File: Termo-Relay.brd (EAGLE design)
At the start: 53 x 75.6 mm, 45 parts, among them CN3 PBS-2-VERTICAL, CN5 PBS-4-VERTICAL, IC1 74HCT595D, IC2 74HCT595D, IC3 STM8S103FP, Q2 20M, T1 2N2222, T2 2N2222, T3 2N2222, T4 2N2222

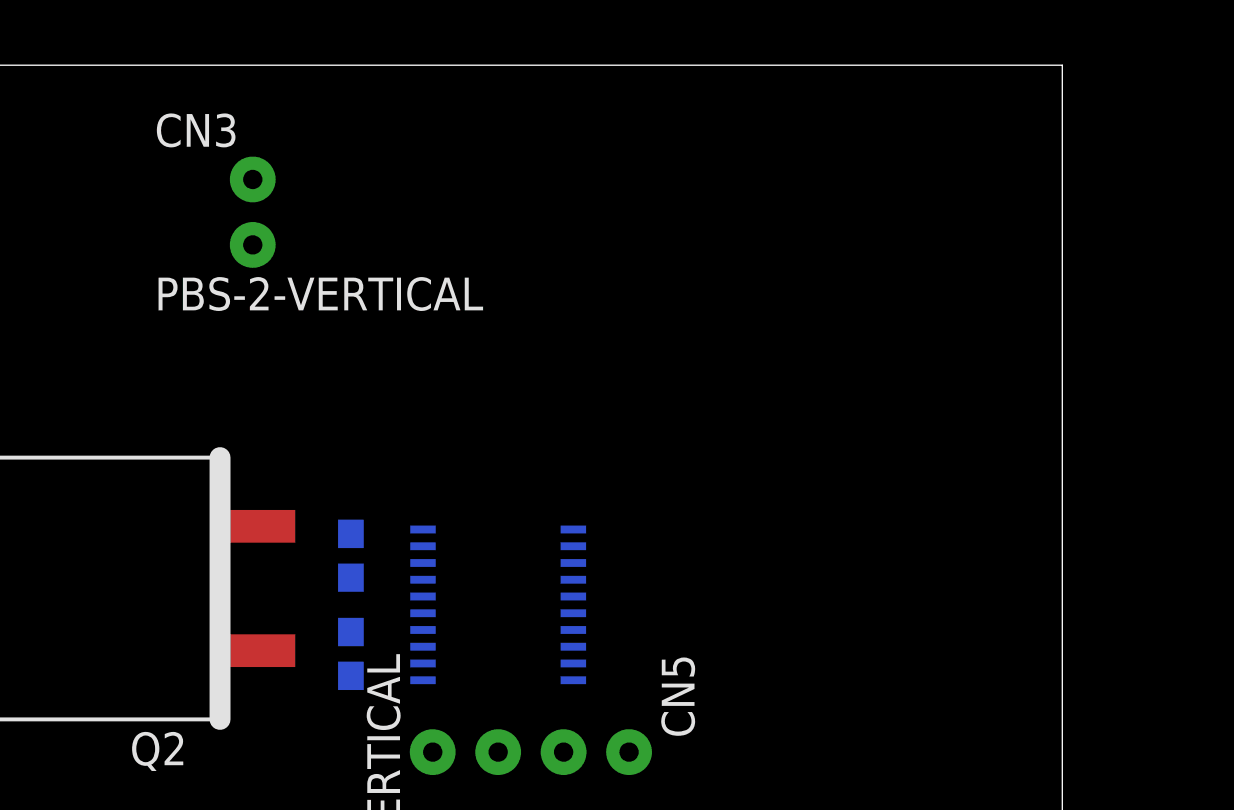
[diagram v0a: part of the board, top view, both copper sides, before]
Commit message: Pins for sensor and heater was added on the scheme. Routes for crystal was added on the pcb.
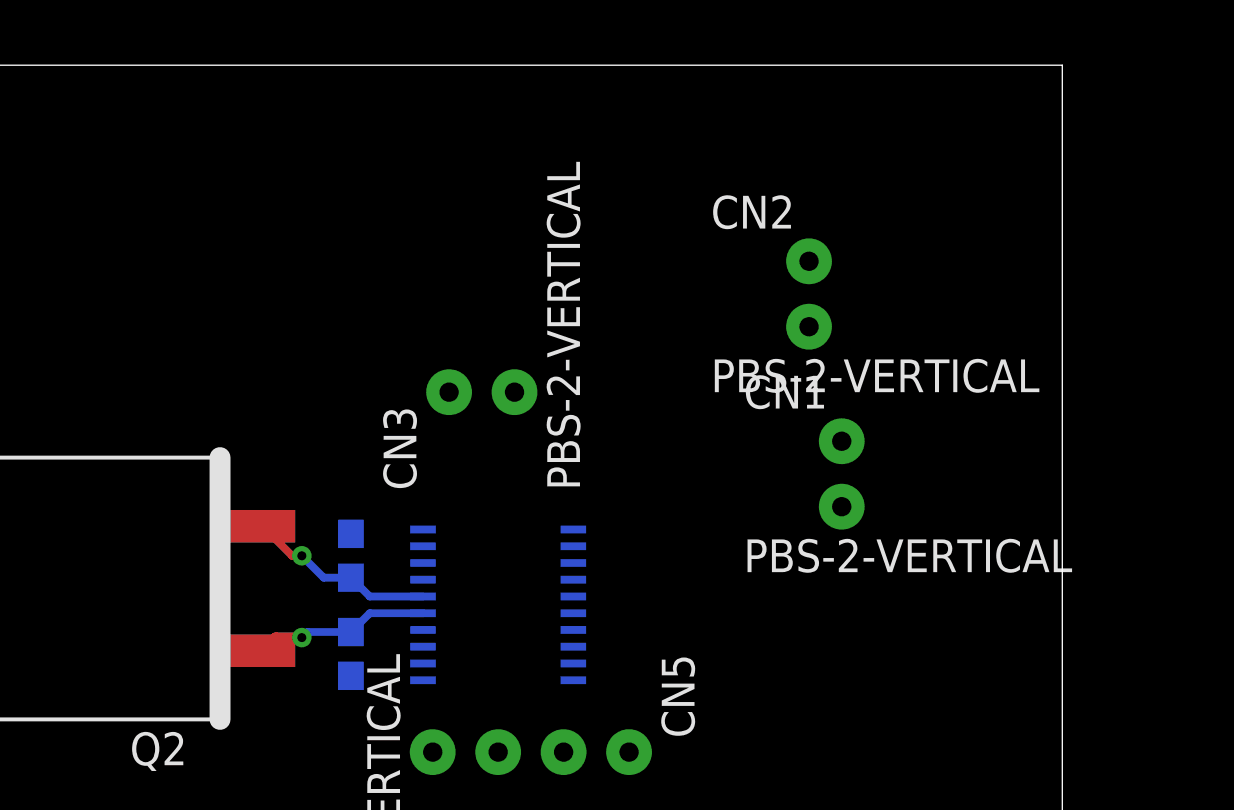
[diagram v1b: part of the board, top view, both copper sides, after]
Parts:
- added CN1, CN2: PBS-2-VERTICAL, pls:PBS-2-VERTICAL
- moved CN3 11.2 mm to (29.2, 62.9), turned to 90 degrees
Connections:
- new net N$18: CN1.P$1, IC3.3
- new net N$20: CN2.P$2, IC3.10
- net BTN_CENTER: no longer IC3.10
- net GND: now also CN1.P$2, CN2.P$1
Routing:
- net N$9: track 0.00 -> 7.35 mm, vias 0 -> 1
- net N$33: track 0.00 -> 6.83 mm, vias 0 -> 1
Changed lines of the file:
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@@
 <element name="C3" library="resistor" library_urn="urn:adsk.eagle:library:348" package="C0603" package3d_urn="urn:adsk.eagle:package:26138/1" value="14p" x="25.4" y="52.705" rot="MR90"/>
 <element name="C4" library="resistor" library_urn="urn:adsk.eagle:library:348" package="C0603" package3d_urn="urn:adsk.eagle:package:26138/1" value="14p" x="25.4" y="56.515" rot="MR270"/>
-<element name="CN3" library="pls" package="PBS-2-VERTICAL" value="PBS-2-VERTICAL" x="21.59" y="71.12"/>
+<element name="CN3" library="pls" package="PBS-2-VERTICAL" value="PBS-2-VERTICAL" x="29.21" y="62.865" rot="R90"/>
 <element name="CN5" library="pls" package="PBS-4-VERTICAL" value="PBS-4-VERTICAL" x="36.195" y="48.895" rot="R270"/>
 <element name="IC1" library="74xx-eu" library_urn="urn:adsk.eagle:library:85" package="SO16" package3d_urn="urn:adsk.eagle:package:2010/1" value="74HCT595D" x="33.02" y="14.605" rot="MR180"/>
@@
 <element name="DISPLAY1" library="PK-7SegmentIndicator" package="7SEG-4DIGITS" value="7SEGS-4DIGITS" x="36.195" y="30.48" rot="R270"/>
 <element name="R1" library="resistor" library_urn="urn:adsk.eagle:library:348" package="R0603" package3d_urn="urn:adsk.eagle:package:26057/1" value="33" x="33.655" y="22.225" rot="MR270"/>
+<element name="CN1" library="pls" package="PBS-2-VERTICAL" value="PBS-2-VERTICAL" x="44.45" y="60.96"/>
+<element name="CN2" library="pls" package="PBS-2-VERTICAL" value="PBS-2-VERTICAL" x="43.18" y="67.945"/>
 </elements>
 <signals>
@@
 <wire x1="31.75" y1="9.525" x2="32.385" y2="10.16" width="0.4" layer="16"/>
 <wire x1="32.385" y1="10.16" x2="32.385" y2="11.5316" width="0.4" layer="16"/>
-<wire x1="25.4" y1="57.365" x2="21.59" y2="68.58" width="0" layer="19" extent="16-16"/>
+<contactref element="CN2" pad="P$1"/>
+<contactref element="CN1" pad="P$2"/>
+<wire x1="25.4" y1="57.365" x2="31.75" y2="62.865" width="0" layer="19" extent="16-16"/>
 <wire x1="28.1972" y1="55.585" x2="25.4" y2="57.365" width="0" layer="19" extent="16-16"/>
 <wire x1="25.4" y1="51.855" x2="28.1972" y2="55.585" width="0" layer="19" extent="16-16"/>
@@
 <wire x1="37.465" y1="17.6784" x2="32.385" y2="11.5316" width="0" layer="19" extent="16-16"/>
 <wire x1="25.4" y1="17.6784" x2="20.32" y2="11.5316" width="0" layer="19" extent="16-16"/>
+<wire x1="44.45" y1="58.42" x2="5.08" y2="5.08" width="0" layer="19" extent="1-1"/>
+<wire x1="43.18" y1="67.945" x2="44.45" y2="58.42" width="0" layer="19" extent="1-1"/>
 </signal>
 <signal name="VCC">
@@
 <wire x1="16.51" y1="16.383" x2="16.51" y2="8.89" width="0.4" layer="1"/>
 <wire x1="28.575" y1="13.335" x2="28.575" y2="10.795" width="0.4" layer="1"/>
-<wire x1="28.1972" y1="56.885" x2="21.59" y2="71.12" width="0" layer="19" extent="16-16"/>
+<wire x1="28.1972" y1="56.885" x2="29.21" y2="62.865" width="0" layer="19" extent="16-16"/>
 <wire x1="36.195" y1="48.895" x2="28.1972" y2="56.885" width="0" layer="19" extent="16-16"/>
 <wire x1="38.1" y1="30.015" x2="36.195" y2="48.895" width="0" layer="19" extent="1-1"/>
@@
 <contactref element="BTN2" pad="1"/>
 <contactref element="R12" pad="2"/>
-<contactref element="IC3" pad="10"/>
 <wire x1="42.418" y1="11.43" x2="42.838" y2="11.215" width="0.4" layer="1"/>
 <wire x1="42.838" y1="11.215" x2="44.45" y2="11.215" width="0.4" layer="1"/>
 <wire x1="42.418" y1="11.43" x2="40.64" y2="11.43" width="0.4" layer="1"/>
-<wire x1="40.64" y1="11.43" x2="28.1972" y2="57.535" width="0" layer="19" extent="1-16"/>
 <via x="40.64" y="11.43" extent="1-16" drill="0.35"/>
 </signal>
@@
 <contactref element="C4" pad="2"/>
 <contactref element="IC3" pad="6"/>
-<wire x1="28.1972" y1="54.935" x2="21.971" y2="57.658" width="0" layer="19" extent="1-1"/>
-<wire x1="25.4" y1="55.665" x2="28.1972" y2="54.935" width="0" layer="19" extent="1-1"/>
 <contactref element="Q2" pad="2"/>
+<wire x1="25.4" y1="55.665" x2="26.13" y2="54.935" width="0.3" layer="16"/>
+<wire x1="26.13" y1="54.935" x2="28.1972" y2="54.935" width="0.3" layer="16"/>
+<wire x1="21.971" y1="57.658" x2="23.114" y2="56.515" width="0.3" layer="1"/>
+<wire x1="23.114" y1="56.515" x2="23.495" y2="56.515" width="0.3" layer="1"/>
+<via x="23.495" y="56.515" extent="1-16" drill="0.35"/>
+<wire x1="24.345" y1="55.665" x2="25.4" y2="55.665" width="0.3" layer="16"/>
+<wire x1="23.495" y1="56.515" x2="24.345" y2="55.665" width="0.3" layer="16"/>
 </signal>
 <signal name="N$33">
 <contactref element="C3" pad="2"/>
 <contactref element="IC3" pad="5"/>
-<wire x1="28.1972" y1="54.285" x2="25.4" y2="53.555" width="0" layer="19" extent="1-1"/>
-<wire x1="21.971" y1="52.832" x2="28.1972" y2="54.285" width="0" layer="19" extent="1-1"/>
 <contactref element="Q2" pad="1"/>
+<wire x1="21.971" y1="52.832" x2="22.479" y2="53.34" width="0.4" layer="1"/>
+<wire x1="22.479" y1="53.34" x2="23.495" y2="53.34" width="0.4" layer="1"/>
+<via x="23.495" y="53.34" extent="1-16" drill="0.35"/>
+<wire x1="23.495" y1="53.34" x2="23.71" y2="53.555" width="0.3" layer="16"/>
+<wire x1="23.71" y1="53.555" x2="25.4" y2="53.555" width="0.3" layer="16"/>
+<wire x1="25.4" y1="53.555" x2="26.13" y2="54.285" width="0.3" layer="16"/>
+<wire x1="26.13" y1="54.285" x2="28.1972" y2="54.285" width="0.3" layer="16"/>
 </signal>
 <signal name="INDIC-A">
@@
 <wire x1="33.655" y1="23.075" x2="33.655" y2="25.4" width="0.4" layer="16"/>
 </signal>
+<signal name="N$18">
+<contactref element="IC3" pad="3"/>
+<contactref element="CN1" pad="P$1"/>
+<wire x1="44.45" y1="60.96" x2="28.1972" y2="52.985" width="0" layer="19" extent="16-16"/>
+</signal>
+<signal name="N$20">
+<contactref element="IC3" pad="10"/>
+<contactref element="CN2" pad="P$2"/>
+<wire x1="43.18" y1="65.405" x2="28.1972" y2="57.535" width="0" layer="19" extent="16-16"/>
+</signal>
 </signals>

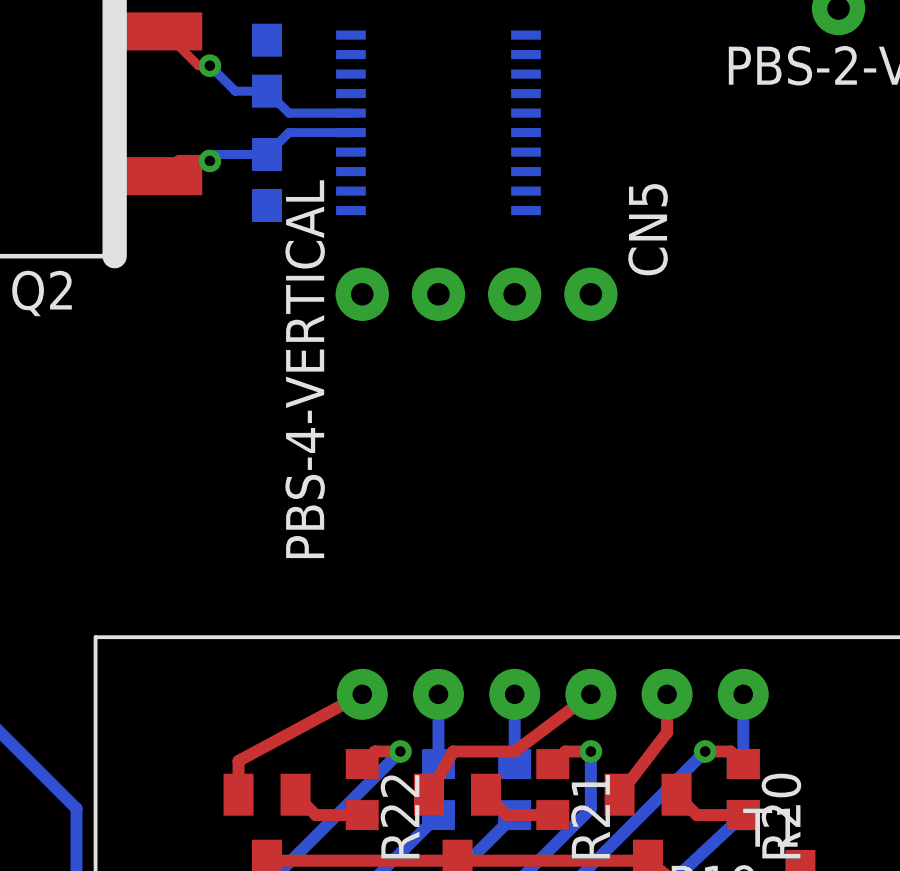
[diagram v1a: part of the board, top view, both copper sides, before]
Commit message: Pins for sensor and heater was added on the scheme. Routes for crystal was added on the pcb.
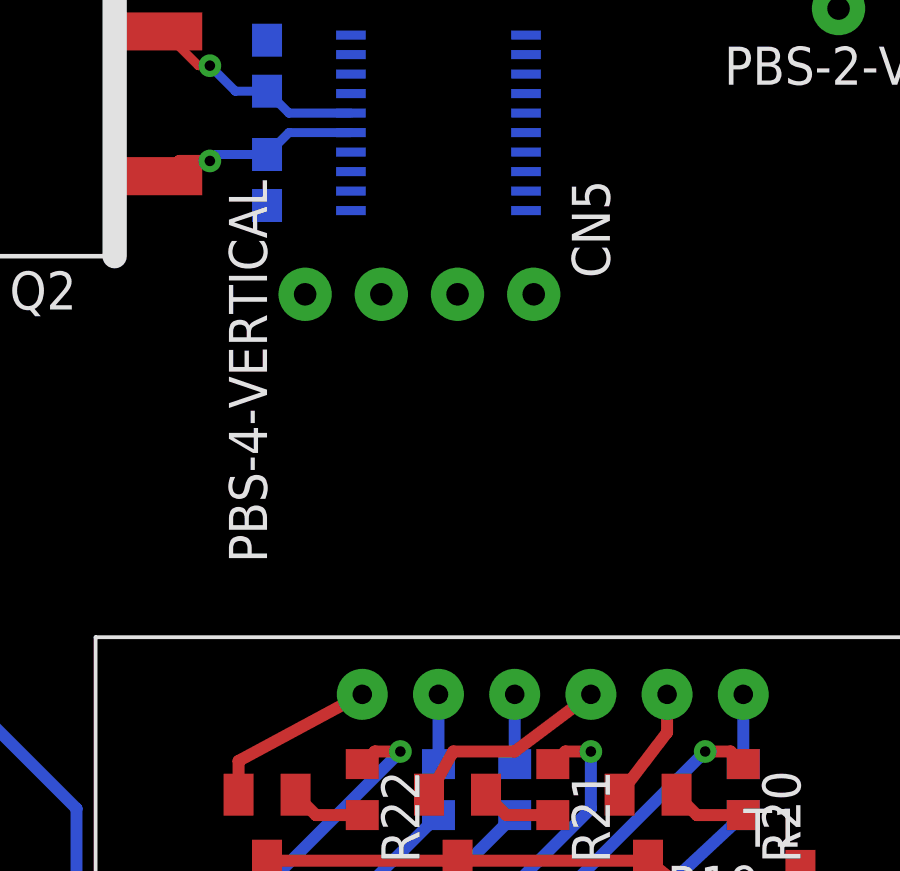
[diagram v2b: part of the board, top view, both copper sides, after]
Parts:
- moved CN5 1.91 mm to (34.3, 48.9)
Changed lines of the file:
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@@
 <element name="C4" library="resistor" library_urn="urn:adsk.eagle:library:348" package="C0603" package3d_urn="urn:adsk.eagle:package:26138/1" value="14p" x="25.4" y="56.515" rot="MR270"/>
 <element name="CN3" library="pls" package="PBS-2-VERTICAL" value="PBS-2-VERTICAL" x="29.21" y="62.865" rot="R90"/>
-<element name="CN5" library="pls" package="PBS-4-VERTICAL" value="PBS-4-VERTICAL" x="36.195" y="48.895" rot="R270"/>
+<element name="CN5" library="pls" package="PBS-4-VERTICAL" value="PBS-4-VERTICAL" x="34.29" y="48.895" rot="R270"/>
 <element name="IC1" library="74xx-eu" library_urn="urn:adsk.eagle:library:85" package="SO16" package3d_urn="urn:adsk.eagle:package:2010/1" value="74HCT595D" x="33.02" y="14.605" rot="MR180"/>
 <element name="IC2" library="74xx-eu" library_urn="urn:adsk.eagle:library:85" package="SO16" package3d_urn="urn:adsk.eagle:package:2010/1" value="74HCT595D" x="20.955" y="14.605" rot="MR180"/>
@@
 <wire x1="28.1972" y1="55.585" x2="25.4" y2="57.365" width="0" layer="19" extent="16-16"/>
 <wire x1="25.4" y1="51.855" x2="28.1972" y2="55.585" width="0" layer="19" extent="16-16"/>
-<wire x1="28.575" y1="48.895" x2="25.4" y2="51.855" width="0" layer="19" extent="16-16"/>
+<wire x1="26.67" y1="48.895" x2="25.4" y2="51.855" width="0" layer="19" extent="16-16"/>
 <wire x1="8.04" y1="36.83" x2="25.4" y2="51.855" width="0" layer="19" extent="1-16"/>
 <wire x1="31.75" y1="9.525" x2="32.17" y2="3.81" width="0" layer="19" extent="1-16"/>
@@
 <wire x1="28.575" y1="13.335" x2="28.575" y2="10.795" width="0.4" layer="1"/>
 <wire x1="28.1972" y1="56.885" x2="29.21" y2="62.865" width="0" layer="19" extent="16-16"/>
-<wire x1="36.195" y1="48.895" x2="28.1972" y2="56.885" width="0" layer="19" extent="16-16"/>
-<wire x1="38.1" y1="30.015" x2="36.195" y2="48.895" width="0" layer="19" extent="1-1"/>
+<wire x1="34.29" y1="48.895" x2="28.1972" y2="56.885" width="0" layer="19" extent="16-16"/>
+<wire x1="38.1" y1="30.015" x2="34.29" y2="48.895" width="0" layer="19" extent="1-1"/>
 <wire x1="35.433" y1="19.05" x2="38.905" y2="29.38" width="0" layer="19" extent="1-1"/>
 </signal>
@@
 <contactref element="IC3" pad="18"/>
 <contactref element="CN5" pad="P$2"/>
-<wire x1="34.0328" y1="52.985" x2="33.655" y2="48.895" width="0" layer="19" extent="1-1"/>
+<wire x1="34.0328" y1="52.985" x2="31.75" y2="48.895" width="0" layer="19" extent="1-1"/>
 </signal>
 <signal name="N$19">
 <contactref element="IC3" pad="4"/>
 <contactref element="CN5" pad="P$3"/>
-<wire x1="28.1972" y1="53.635" x2="31.115" y2="48.895" width="0" layer="19" extent="1-1"/>
+<wire x1="28.1972" y1="53.635" x2="29.21" y2="48.895" width="0" layer="19" extent="1-1"/>
 </signal>
 <signal name="INDIC-DP">

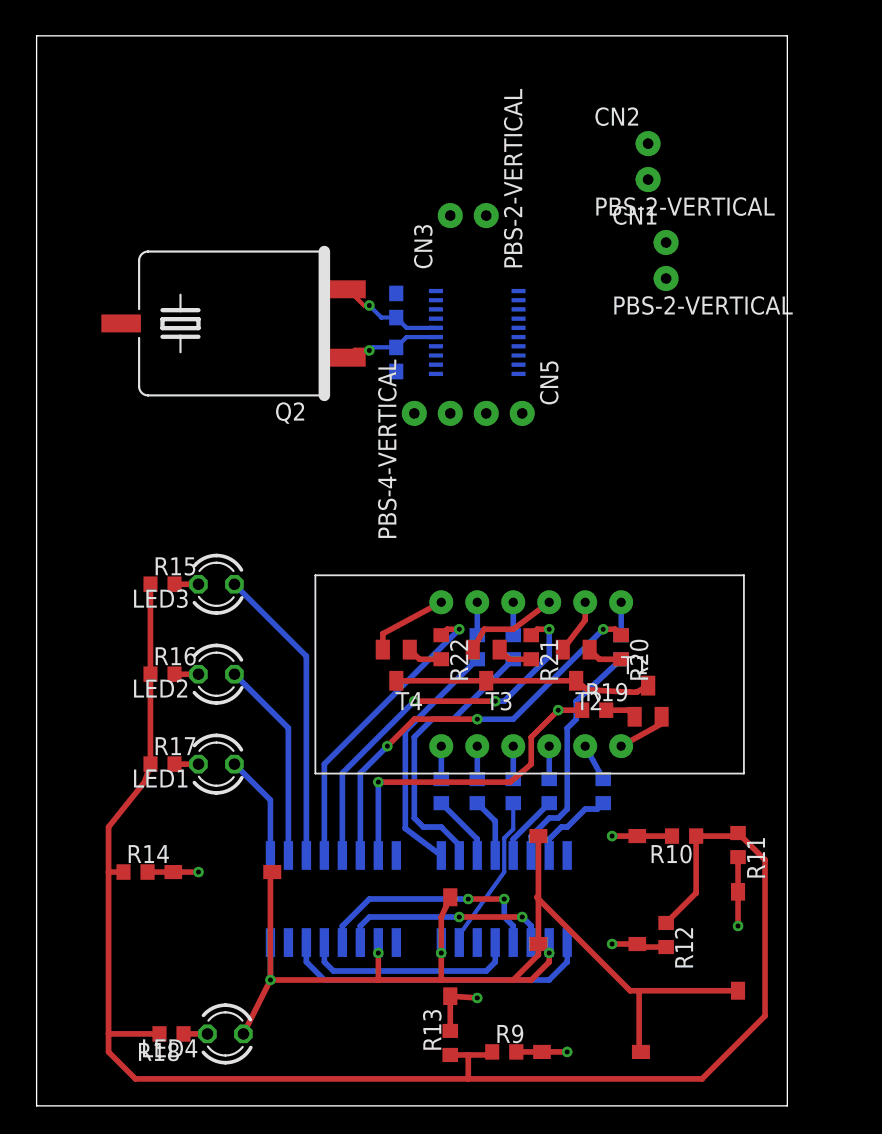
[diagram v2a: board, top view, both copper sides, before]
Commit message: Capaxcitors were added/ PCB routers for stym8 were added
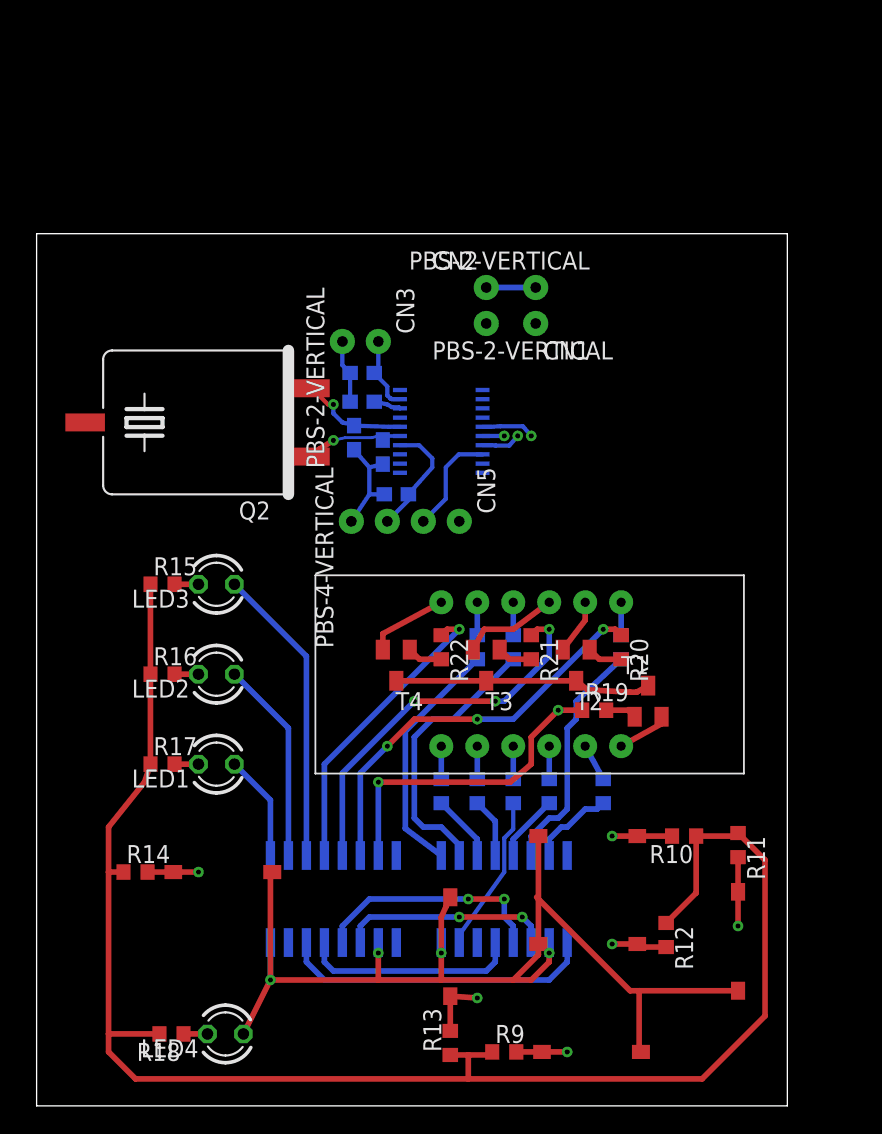
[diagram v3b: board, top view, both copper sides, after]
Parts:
- added C1: 0.1u, resistor:C0603
- added C2: 470-3300n, resistor:C0603
- added C5: 1u, resistor:C0603
- Q2: value 20M -> 16M
- moved CN2 15.3 mm to (31.8, 57.8)
- moved CN1 10.8 mm to (35.2, 55.2), turned to 180 degrees
- moved CN3 10.2 mm to (24.1, 54.0), turned to 270 degrees
- moved C4 9.80 mm to (22.4, 47.2), turned to 90 degrees
- moved CN5 8.82 mm to (29.8, 41.3)
- moved IC3 7.43 mm to (28.6, 47.6)
- moved Q2 7.43 mm to (11.4, 48.3)
- moved C3 6.61 mm to (24.4, 46.2)
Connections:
- removed net VCAP: IC3.8
- new net N$21: C2.2, IC3.8
- net GND: now also C1.1, C2.1, C5.1
- net N$19: now also C1.2
- net VCC: now also C5.2
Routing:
- net GND: track 131.5 -> 147.3 mm
- net N$19: track 0.00 -> 8.37 mm
- net N$17: track 0.00 -> 7.45 mm
- net VCC: track 96.0 -> 101.3 mm
- net RCK: track 16.7 -> 20.5 mm, vias 2 -> 3
- net SER: track 0.74 -> 3.53 mm, vias 0 -> 1
- net N$21: track 0.00 -> 1.92 mm
- net SCK: track 14.9 -> 16.5 mm, vias 2 -> 3
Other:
- board size 53 x 75.6 mm -> 53 x 61.6 mm
